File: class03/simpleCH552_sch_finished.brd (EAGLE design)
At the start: 40.6 x 12 mm, 12 parts, among them U1 CH552G, X1 USBPCB

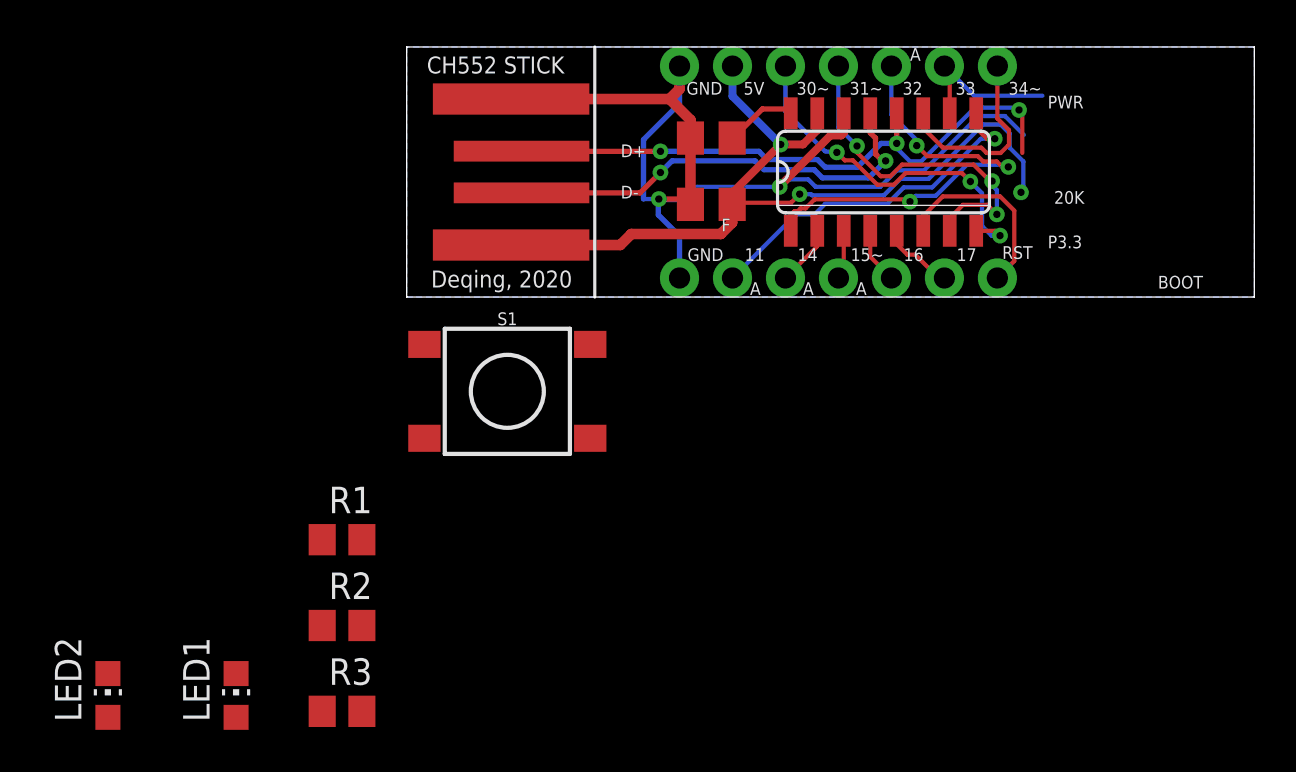
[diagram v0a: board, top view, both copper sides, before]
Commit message: update to USB shell model
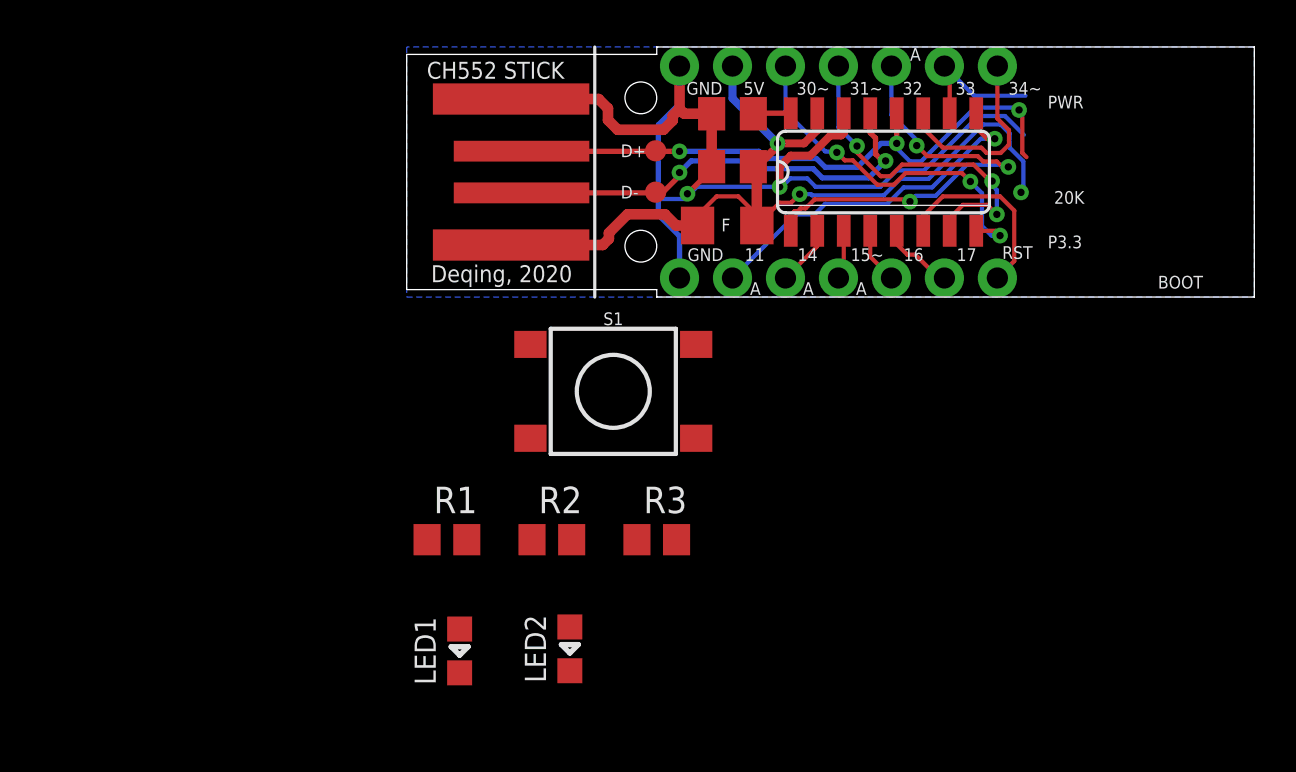
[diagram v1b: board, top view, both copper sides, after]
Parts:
- added F1: (no value), adafruit:R1206
- added TP1, TP2: TEST-POINT3X4, SparkFun-Connectors:PAD.03X.04
- LED1: value RED -> PWR; device led:CHIP-LED0805 -> BeagleBone_Black_Wireless:GHI-BASICCOMPONENTS_0805-LED
- LED2: value GREEN -> P3.3; device led:CHIP-LED0805 -> BeagleBone_Black_Wireless:GHI-BASICCOMPONENTS_0805-LED
- moved LED2 22.3 mm to (7.82, -16.9)
- moved R3 17.2 mm to (12.0, -11.6)
- moved LED1 10.9 mm to (2.54, -17.0)
- moved R2 10.9 mm to (6.96, -11.6)
- moved S1 5.08 mm to (9.91, -4.52)
- moved R1 5.03 mm to (1.93, -11.6)
- moved C1 2.07 mm to (15.6, 6.25)
- moved C2 1.55 mm to (15.6, 8.79)
- renumbered U1 to U2
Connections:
- net +5V: now also F1.1, F1.2
- net GND: now also LED1.K, LED2.K; no longer LED1.C, LED2.C
- net USB_D+: now also TP2.P$1
- net USB_D-: now also TP1.P$1
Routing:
- net +5V: track 41.6 -> 43.8 mm
- net 3.3V: track 3.46 -> 1.80 mm
- net USB_D+: track 29.8 -> 31.3 mm
- net P3.3: track 7.65 -> 6.84 mm
- net GND: track 53.5 -> 54.1 mm
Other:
- outline, holes or cut-outs redrawn
- board text added: "Deqing Sun, 2020 Try Ch55xduino with this board"
- board text added: "Deqing Sun, 2022 Prototyping Electronic Devices"
- board text removed: "Deqing Sun, 2020 Prototyping Electronic Devices"
